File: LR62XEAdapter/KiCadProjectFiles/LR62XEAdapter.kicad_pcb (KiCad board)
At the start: 2 copper layers, 24 x 36.8 mm, 2 parts, among them J1 Conn_01x23_Socket, U1 LR62XE

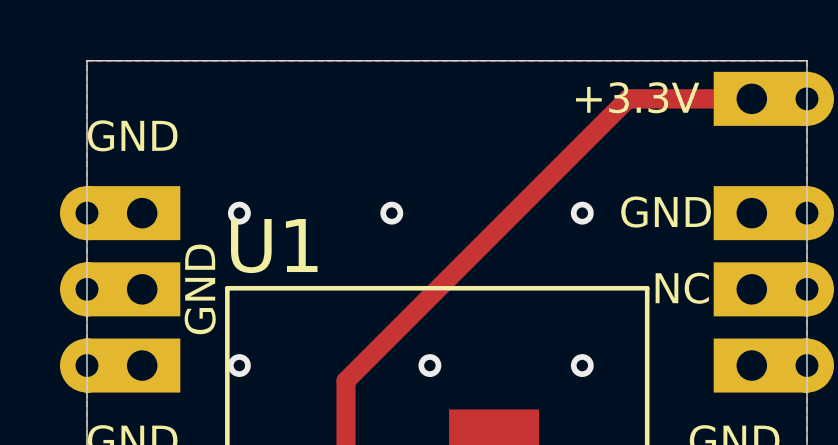
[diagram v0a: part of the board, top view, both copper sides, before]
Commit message: added adapter pictures, changed adapter silkscreen
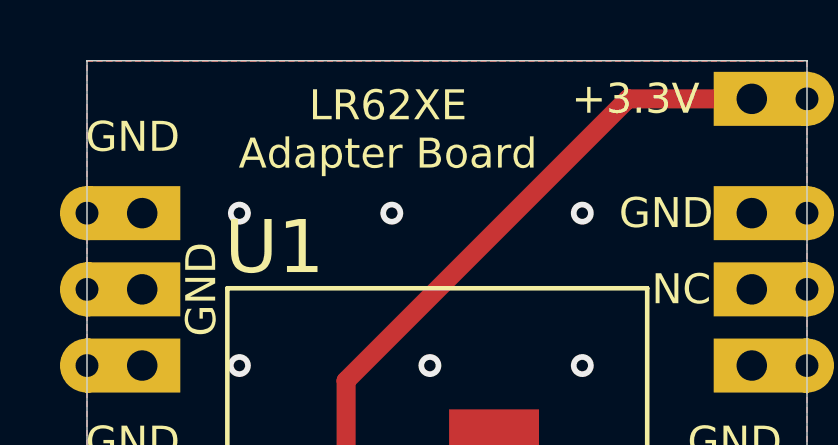
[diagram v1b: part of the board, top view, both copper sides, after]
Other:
- board text added: "LR62XE Adapter Board"
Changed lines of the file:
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@@
+		)
+	)
+	(gr_text "LR62XE \nAdapter Board"
+		(at 99.633 45.623 0)
+		(layer "F.SilkS")
+		(effects
+			(font
+				(size 1 1)
+				(thickness 0.1)
+			)
+			(justify bottom)
 		)
 	)
